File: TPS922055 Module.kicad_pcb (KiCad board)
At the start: 4 copper layers, 36.7 x 19 mm, 26 parts, among them J1 Conn_01x04_Pin, J2 Conn_01x04_Pin, J3 Conn_01x02_Pin, U1 TPS922055DRRR

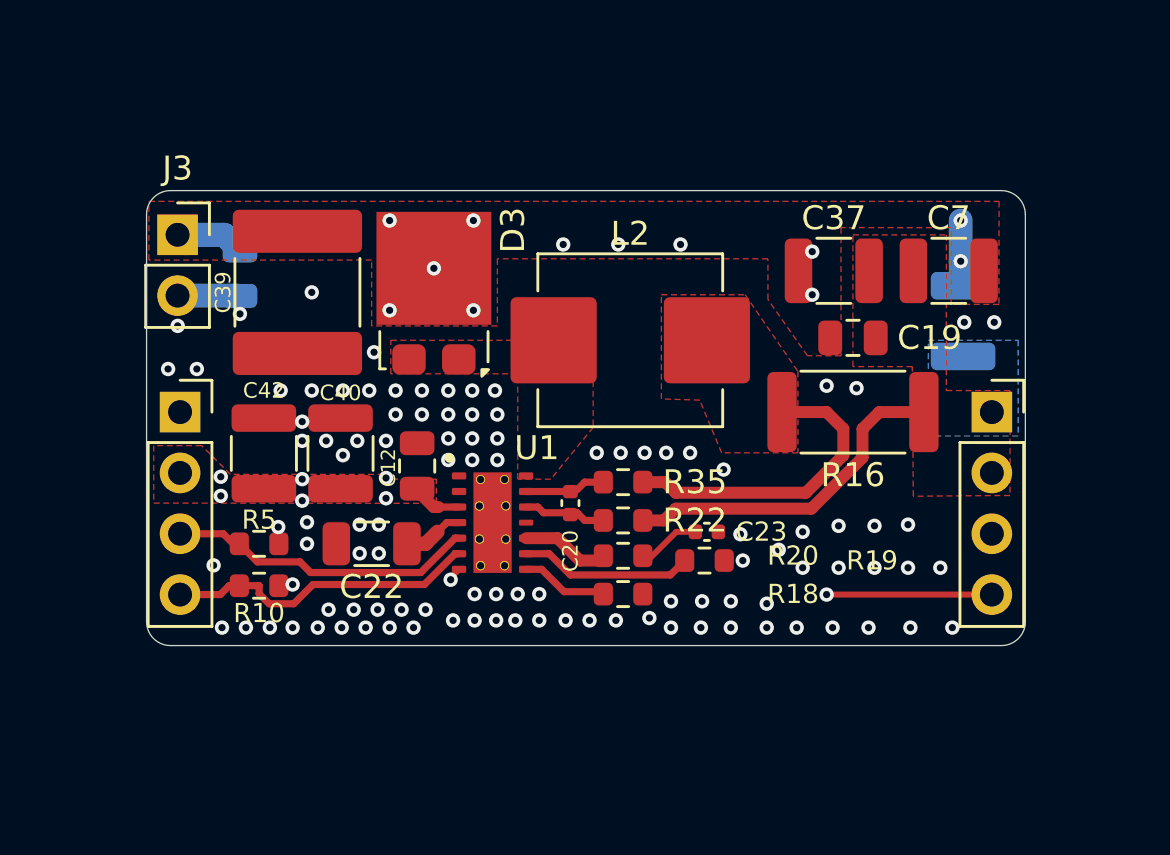
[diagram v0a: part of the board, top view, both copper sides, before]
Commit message: Refinements, Increased module size to fit heatsink better
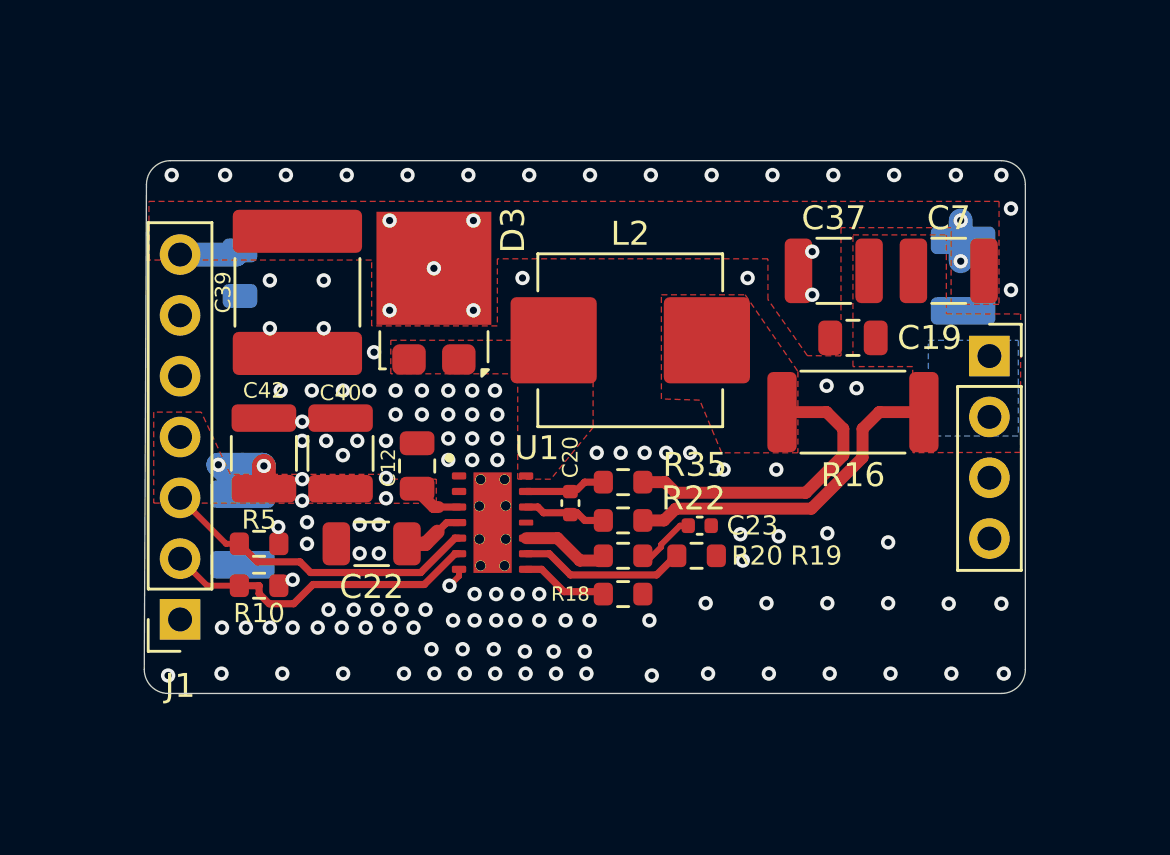
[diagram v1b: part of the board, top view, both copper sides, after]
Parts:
- removed J3: Conn_01x02_Pin, Connector_PinSocket_2.54mm:PinSocket_1x02_P2.54mm_Vertical
- added C41: 10uF, Capacitor_SMD:C_1210_3225Metric, B.Cu at (152.1, 90.9)
- added G***: LOGO, LOGO, B.Cu at (152.0, 81.8)
- J1: value Conn_01x04_Pin -> Conn_01x07_Socket; footprint Connector_PinSocket_2.54mm:PinSocket_1x04_P2.54mm_Vertical -> Connector_PinSocket_2.54mm:PinSocket_1x07_P2.54mm_Vertical
- moved J1 8.66 mm to (149.5, 94.7), turned to 180 degrees
- moved J2 2.34 mm to (183.3, 83.7)
- moved C38 1.90 mm to (182.2, 80.3)
- moved C23 0.40 mm to (171.2, 90.7)
- moved R19 0.39 mm to (171.1, 92.0)
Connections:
- J1 pad 1: GND -> LED_FAULT
- J1 pad 2: VCC -> PWM_EN
- J1 pad 4: PWM_EN -> VCC
- J2 pad 4: /LED_FAULT -> VCC
- U1 pad 7: /LED_FAULT -> LED_FAULT
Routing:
- net /LED_FAULT: track 23.4 -> 0.00 mm, vias 2 -> 0
- net LED_FAULT: track 0.00 -> 12.7 mm, vias 0 -> 1
- net VCC: track 9.14 -> 14.7 mm
- net GND: track 8.41 -> 5.90 mm, vias 106 -> 128
- net PWM_ADIM: track 13.0 -> 13.5 mm
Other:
- board size 36.7 x 19 mm -> 36.8 x 22.2 mm
- board text added: "TPS922055 V1.0"
